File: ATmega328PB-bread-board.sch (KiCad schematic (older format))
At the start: 6 parts, among them J1 Conn_01x17, J2 Conn_01x17, U1 ATmega328PB-MU

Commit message: Add DTR pin and change pin layout
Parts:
- added C3: 0.1uf, Capacitor_SMD:C_0402_1005Metric, symbol ATmega328PB-bread-board-rescue:C-Device
- C1, C2: footprint Capacitor_SMD:C_0603_1608Metric -> Capacitor_SMD:C_0402_1005Metric; symbol Device:C -> ATmega328PB-bread-board-rescue:C-Device
- J1, J2: symbol Connector_Generic:Conn_01x17 -> ATmega328PB-bread-board-rescue:Conn_01x17-Connector_Generic
- JP1: symbol Device:Jumper_NC_Small -> ATmega328PB-bread-board-rescue:Jumper_NC_Small-Device
- U1: symbol MCU_Microchip_ATmega:ATmega328PB-MU -> ATmega328PB-bread-board-rescue:ATmega328PB-MU-MCU_Microchip_ATmega
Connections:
- net GND: no longer J2.1 (Pin_1)
- net pb5: now also J2.1 (Pin_1); no longer J2.2 (Pin_2)
- net pb6: now also J2.8 (Pin_8); no longer J2.9 (Pin_9)
- net pb7: now also J2.9 (Pin_9); no longer J2.10 (Pin_10)
- net pc0: now also J2.2 (Pin_2); no longer J2.3 (Pin_3)
- net pc1: now also J2.3 (Pin_3); no longer J2.4 (Pin_4)
- net pc2: now also J2.4 (Pin_4); no longer J2.5 (Pin_5)
- net pc3: now also J2.5 (Pin_5); no longer J2.6 (Pin_6)
- net pc4: now also J2.6 (Pin_6); no longer J2.7 (Pin_7)
- net pc5: now also J2.7 (Pin_7); no longer J2.8 (Pin_8)
- net pc6: now also J2.10 (Pin_10), C3.2; no longer J1.1 (Pin_1)
- net pd0: now also J1.3 (Pin_3); no longer J1.2 (Pin_2)
- net pd1: now also J1.2 (Pin_2); no longer J1.3 (Pin_3)
- new net DTR: C3.1, J1.1 (Pin_1)
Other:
- moved on the sheet: J1, J2
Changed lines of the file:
@@
 $EndDescr
 $Comp
-L power:VCC #PWR0101
+L ATmega328PB-bread-board-rescue:VCC-power #PWR0101
 U 1 1 5EEFD2BC
 P 4800 1850
@@
 aref
 $Comp
-L Device:C C1
+L ATmega328PB-bread-board-rescue:C-Device C1
 U 1 1 5EEFE1E4
 P 3950 2850
 F 0 "C1" H 4065 2896 50  0000 L CNN
 F 1 "0.1uf" H 4065 2805 50  0000 L CNN
-F 2 "Capacitor_SMD:C_0603_1608Metric" H 3988 2700 50  0001 C CNN
+F 2 "Capacitor_SMD:C_0402_1005Metric" H 3988 2700 50  0001 C CNN
 F 3 "~" H 3950 2850 50  0001 C CNN
 	1    3950 2850
@@
 	3950 2700 3800 2700
 $Comp
-L power:GND #PWR0102
+L ATmega328PB-bread-board-rescue:GND-power #PWR0102
 U 1 1 5EEFCEDC
 P 4800 5400
@@
 $EndComp
 $Comp
-L power:GND #PWR0103
+L ATmega328PB-bread-board-rescue:GND-power #PWR0103
 U 1 1 5EEFF77C
 P 3950 3000
@@
 pe3
 $Comp
-L Device:C C2
+L ATmega328PB-bread-board-rescue:C-Device C2
 U 1 1 5EF038C7
 P 4400 2000
 F 0 "C2" H 4515 2046 50  0000 L CNN
 F 1 "0.1uf" H 4515 1955 50  0000 L CNN
-F 2 "Capacitor_SMD:C_0603_1608Metric" H 4438 1850 50  0001 C CNN
+F 2 "Capacitor_SMD:C_0402_1005Metric" H 4438 1850 50  0001 C CNN
 F 3 "~" H 4400 2000 50  0001 C CNN
 	1    4400 2000
@@
 	4800 1850 4800 2150
 $Comp
-L power:GND #PWR0104
+L ATmega328PB-bread-board-rescue:GND-power #PWR0104
 U 1 1 5EF066FF
 P 4400 2150
@@
 	1    0    0    -1
 $EndComp
-Text Label 6600 2950 0    50   ~ 0
+Text Label 7550 3000 0    50   ~ 0
 pd0
-Text Label 6600 3050 0    50   ~ 0
+Text Label 7550 2900 0    50   ~ 0
 pd1
 $Comp
-L Device:Jumper_NC_Small JP1
+L ATmega328PB-bread-board-rescue:Jumper_NC_Small-Device JP1
 U 1 1 5EF1D9B3
 P 4900 2150
@@
 	4900 2300 4900 2400
 $Comp
-L power:GND #PWR0105
+L ATmega328PB-bread-board-rescue:GND-power #PWR0105
 U 1 1 5EF20D84
-P 7550 4350
-F 0 "#PWR0105" H 7550 4100 50  0001 C CNN
-F 1 "GND" H 7555 4177 50  0000 C CNN
-F 2 "" H 7550 4350 50  0001 C CNN
-F 3 "" H 7550 4350 50  0001 C CNN
-	1    7550 4350
-	1    0    0    -1
-$EndComp
-$Comp
-L Connector_Generic:Conn_01x17 J1
+P 8500 4300
+F 0 "#PWR0105" H 8500 4050 50  0001 C CNN
+F 1 "GND" H 8505 4127 50  0000 C CNN
+F 2 "" H 8500 4300 50  0001 C CNN
+F 3 "" H 8500 4300 50  0001 C CNN
+	1    8500 4300
+	1    0    0    -1
+$EndComp
+$Comp
+L ATmega328PB-bread-board-rescue:Conn_01x17-Connector_Generic J1
 U 1 1 5EF236D3
-P 6400 3650
-F 0 "J1" H 6318 4667 50  0000 C CNN
-F 1 "Conn_01x17" H 6318 4576 50  0000 C CNN
-F 2 "Connector_PinSocket_2.54mm:PinSocket_1x17_P2.54mm_Vertical" H 6400 3650 50  0001 C CNN
-F 3 "~" H 6400 3650 50  0001 C CNN
-	1    6400 3650
+P 7350 3600
+F 0 "J1" H 7268 4617 50  0000 C CNN
+F 1 "Conn_01x17" H 7268 4526 50  0000 C CNN
+F 2 "Connector_PinSocket_2.54mm:PinSocket_1x17_P2.54mm_Vertical" H 7350 3600 50  0001 C CNN
+F 3 "~" H 7350 3600 50  0001 C CNN
+	1    7350 3600
 	-1   0    0    -1
 $EndComp
 $Comp
-L Connector_Generic:Conn_01x17 J2
+L ATmega328PB-bread-board-rescue:Conn_01x17-Connector_Generic J2
 U 1 1 5EF241A6
-P 7350 3550
-F 0 "J2" H 7268 4567 50  0000 C CNN
-F 1 "Conn_01x17" H 7268 4476 50  0000 C CNN
-F 2 "Connector_PinSocket_2.54mm:PinSocket_1x17_P2.54mm_Vertical" H 7350 3550 50  0001 C CNN
-F 3 "~" H 7350 3550 50  0001 C CNN
-	1    7350 3550
+P 8300 3500
+F 0 "J2" H 8218 4517 50  0000 C CNN
+F 1 "Conn_01x17" H 8218 4426 50  0000 C CNN
+F 2 "Connector_PinSocket_2.54mm:PinSocket_1x17_P2.54mm_Vertical" H 8300 3500 50  0001 C CNN
+F 3 "~" H 8300 3500 50  0001 C CNN
+	1    8300 3500
 	-1   0    0    -1
 $EndComp
 $Comp
-L power:GND #PWR0107
+L ATmega328PB-bread-board-rescue:GND-power #PWR0107
 U 1 1 5EF24D90
-P 6900 3250
-F 0 "#PWR0107" H 6900 3000 50  0001 C CNN
-F 1 "GND" H 6905 3077 50  0000 C CNN
-F 2 "" H 6900 3250 50  0001 C CNN
-F 3 "" H 6900 3250 50  0001 C CNN
-	1    6900 3250
-	1    0    0    -1
-$EndComp
-Text Label 7550 2850 0    50   ~ 0
+P 7850 3200
+F 0 "#PWR0107" H 7850 2950 50  0001 C CNN
+F 1 "GND" H 7855 3027 50  0000 C CNN
+F 2 "" H 7850 3200 50  0001 C CNN
+F 3 "" H 7850 3200 50  0001 C CNN
+	1    7850 3200
+	1    0    0    -1
+$EndComp
+Text Label 8500 2700 0    50   ~ 0
 pb5
-Text Label 6600 4450 0    50   ~ 0
+Text Label 7550 4400 0    50   ~ 0
 pb4
-Text Label 6600 4350 0    50   ~ 0
+Text Label 7550 4300 0    50   ~ 0
 pb3
-Text Label 6600 4250 0    50   ~ 0
+Text Label 7550 4200 0    50   ~ 0
 pb2
-Text Label 6600 4150 0    50   ~ 0
+Text Label 7550 4100 0    50   ~ 0
 pb1
-Text Label 6600 4050 0    50   ~ 0
+Text Label 7550 4000 0    50   ~ 0
 pb0
-Text Label 6600 3950 0    50   ~ 0
+Text Label 7550 3900 0    50   ~ 0
 pd7
-Text Label 6600 3850 0    50   ~ 0
+Text Label 7550 3800 0    50   ~ 0
 pd6
-Text Label 6600 3750 0    50   ~ 0
+Text Label 7550 3700 0    50   ~ 0
 pd5
-Text Label 6600 3650 0    50   ~ 0
+Text Label 7550 3600 0    50   ~ 0
 pd4
-Text Label 6600 3550 0    50   ~ 0
+Text Label 7550 3500 0    50   ~ 0
 pd3
-Text Label 6600 3450 0    50   ~ 0
+Text Label 7550 3400 0    50   ~ 0
 pd2
-Text Label 7550 3050 0    50   ~ 0
+Text Label 8500 2900 0    50   ~ 0
 pc1
-Text Label 7550 2950 0    50   ~ 0
+Text Label 8500 2800 0    50   ~ 0
 pc0
-Text Label 7550 4150 0    50   ~ 0
+Text Label 8500 4100 0    50   ~ 0
 aref
-Text Label 7550 4050 0    50   ~ 0
+Text Label 8500 4000 0    50   ~ 0
 pe3
-Text Label 7550 3950 0    50   ~ 0
+Text Label 8500 3900 0    50   ~ 0
 pe2
-Text Label 7550 3850 0    50   ~ 0
+Text Label 8500 3800 0    50   ~ 0
 pe1
-Text Label 7550 3750 0    50   ~ 0
+Text Label 8500 3700 0    50   ~ 0
 pe0
-Text Label 6600 2850 0    50   ~ 0
-pc6
-Text Label 7550 3450 0    50   ~ 0
+Text Label 7550 2800 0    50   ~ 0
+DTR
+Text Label 8500 3300 0    50   ~ 0
 pc5
-Text Label 7550 3350 0    50   ~ 0
+Text Label 8500 3200 0    50   ~ 0
 pc4
-Text Label 7550 3250 0    50   ~ 0
+Text Label 8500 3100 0    50   ~ 0
 pc3
-Text Label 7550 3150 0    50   ~ 0
+Text Label 8500 3000 0    50   ~ 0
 pc2
-Text Label 7550 3650 0    50   ~ 0
+Text Label 8500 3500 0    50   ~ 0
 pb7
-Text Label 7550 3550 0    50   ~ 0
+Text Label 8500 3400 0    50   ~ 0
 pb6
 Wire Wire Line
-	6900 3250 6700 3250
-$Comp
-L power:VCC #PWR0108
+	7850 3200 7650 3200
+$Comp
+L ATmega328PB-bread-board-rescue:VCC-power #PWR0108
 U 1 1 5EF389BE
-P 6900 3150
-F 0 "#PWR0108" H 6900 3000 50  0001 C CNN
-F 1 "VCC" H 6915 3323 50  0000 C CNN
-F 2 "" H 6900 3150 50  0001 C CNN
-F 3 "" H 6900 3150 50  0001 C CNN
-	1    6900 3150
-	1    0    0    -1
-$EndComp
-Wire Wire Line
-	6700 3250 6700 3350
-Wire Wire Line
-	6700 3350 6600 3350
-Connection ~ 6700 3250
-Wire Wire Line
-	6700 3250 6600 3250
-Wire Wire Line
-	6900 3150 6600 3150
-$Comp
-L power:GND #PWR0109
-U 1 1 5EF4FA8E
-P 7850 2750
-F 0 "#PWR0109" H 7850 2500 50  0001 C CNN
-F 1 "GND" H 7855 2577 50  0000 C CNN
-F 2 "" H 7850 2750 50  0001 C CNN
-F 3 "" H 7850 2750 50  0001 C CNN
-	1    7850 2750
-	1    0    0    -1
-$EndComp
-Wire Wire Line
-	7850 2750 7550 2750
-$Comp
-L MCU_Microchip_ATmega:ATmega328PB-MU U1
+P 7850 3100
+F 0 "#PWR0108" H 7850 2950 50  0001 C CNN
+F 1 "VCC" H 7865 3273 50  0000 C CNN
+F 2 "" H 7850 3100 50  0001 C CNN
+F 3 "" H 7850 3100 50  0001 C CNN
+	1    7850 3100
+	1    0    0    -1
+$EndComp
+Wire Wire Line
+	7650 3200 7650 3300
+Wire Wire Line
+	7650 3300 7550 3300
+Connection ~ 7650 3200
+Wire Wire Line
+	7650 3200 7550 3200
+Wire Wire Line
+	7850 3100 7550 3100
+$Comp
+L ATmega328PB-bread-board-rescue:ATmega328PB-MU-MCU_Microchip_ATmega U1
 U 1 1 5EF5772F
 P 4800 3900
@@
 	1    0    0    -1
 $EndComp
-Text Label 7550 4250 0    50   ~ 0
+Text Label 8500 4200 0    50   ~ 0
 avcc
 Text Label 5000 2150 0    50   ~ 0
@@
 Wire Wire Line
 	3950 2700 4200 2700
+$Comp
+L ATmega328PB-bread-board-rescue:C-Device C3
+U 1 1 604E4CAC
+P 5750 4200
+F 0 "C3" V 5850 4300 50  0000 L CNN
+F 1 "0.1uf" V 5650 4300 50  0000 L CNN
+F 2 "Capacitor_SMD:C_0402_1005Metric" H 5788 4050 50  0001 C CNN
+F 3 "~" H 5750 4200 50  0001 C CNN
+	1    5750 4200
+	0    1    1    0
+$EndComp
+Text Label 6100 4200 0    50   ~ 0
+DTR
+Wire Wire Line
+	6100 4200 5900 4200
+Wire Wire Line
+	5600 4200 5400 4200
+Text Label 8500 3600 0    50   ~ 0
+pc6
 $EndSCHEMATC

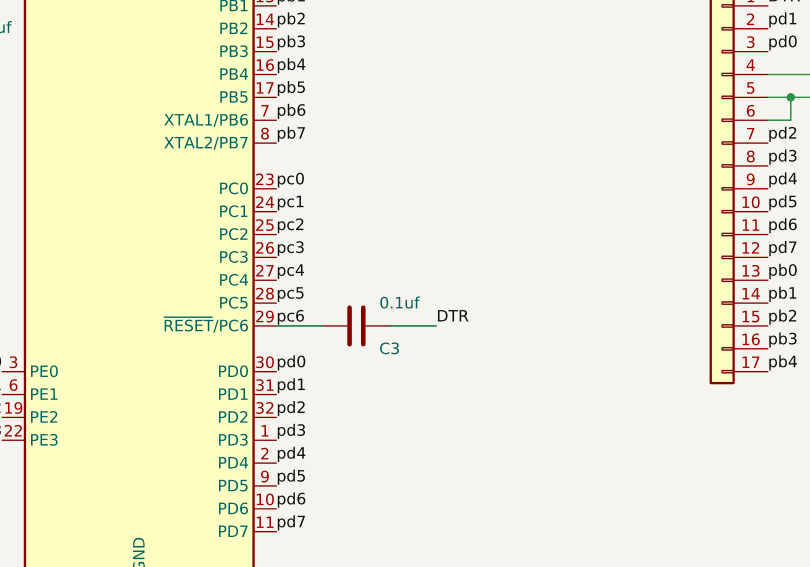
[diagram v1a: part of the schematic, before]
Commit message: Add pullup resistor to RST
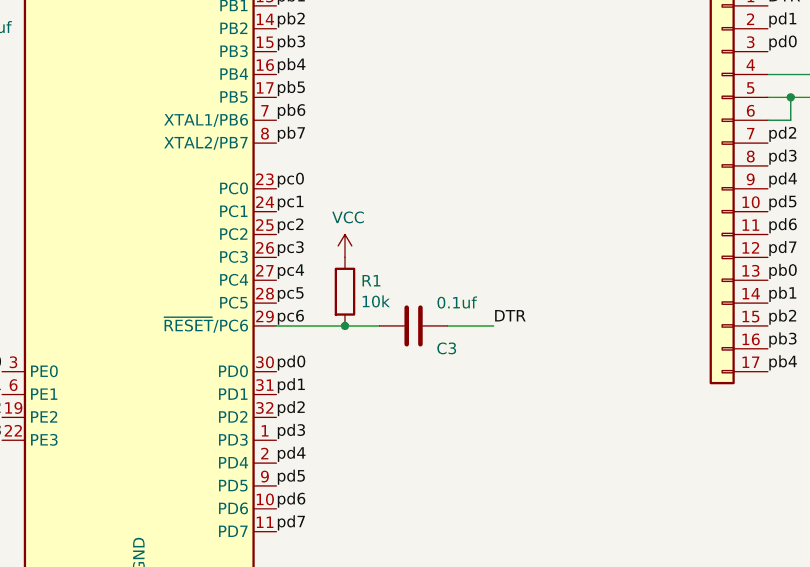
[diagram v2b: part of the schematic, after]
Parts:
- added R1: 10k, Resistor_SMD:R_0603_1608Metric, symbol Device:R
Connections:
- net VCC: now also R1.1
- net pc6: now also R1.2
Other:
- moved on the sheet: C3
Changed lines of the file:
@@
 L ATmega328PB-bread-board-rescue:C-Device C3
 U 1 1 604E4CAC
-P 5750 4200
-F 0 "C3" V 5850 4300 50  0000 L CNN
-F 1 "0.1uf" V 5650 4300 50  0000 L CNN
-F 2 "Capacitor_SMD:C_0402_1005Metric" H 5788 4050 50  0001 C CNN
-F 3 "~" H 5750 4200 50  0001 C CNN
-	1    5750 4200
+P 6000 4200
+F 0 "C3" V 6100 4300 50  0000 L CNN
+F 1 "0.1uf" V 5900 4300 50  0000 L CNN
+F 2 "Capacitor_SMD:C_0402_1005Metric" H 6038 4050 50  0001 C CNN
+F 3 "~" H 6000 4200 50  0001 C CNN
+	1    6000 4200
 	0    1    1    0
 $EndComp
-Text Label 6100 4200 0    50   ~ 0
+Text Label 6350 4200 0    50   ~ 0
 DTR
 Wire Wire Line
-	6100 4200 5900 4200
-Wire Wire Line
-	5600 4200 5400 4200
+	6350 4200 6150 4200
 Text Label 8500 3600 0    50   ~ 0
 pc6
+$Comp
+L Device:R R1
+U 1 1 60746AC4
+P 5700 4050
+F 0 "R1" H 5770 4096 50  0000 L CNN
+F 1 "10k" H 5770 4005 50  0000 L CNN
+F 2 "Resistor_SMD:R_0603_1608Metric" V 5630 4050 50  0001 C CNN
+F 3 "~" H 5700 4050 50  0001 C CNN
+	1    5700 4050
+	1    0    0    -1
+$EndComp
+Wire Wire Line
+	5400 4200 5700 4200
+Connection ~ 5700 4200
+Wire Wire Line
+	5700 4200 5850 4200
+$Comp
+L ATmega328PB-bread-board-rescue:VCC-power #PWR0106
+U 1 1 6074D908
+P 5700 3900
+F 0 "#PWR0106" H 5700 3750 50  0001 C CNN
+F 1 "VCC" H 5715 4073 50  0000 C CNN
+F 2 "" H 5700 3900 50  0001 C CNN
+F 3 "" H 5700 3900 50  0001 C CNN
+	1    5700 3900
+	1    0    0    -1
+$EndComp
 $EndSCHEMATC
